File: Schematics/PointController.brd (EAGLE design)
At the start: 90 x 80 mm, 114 parts, among them IC1 MEGA48/88/168-AU

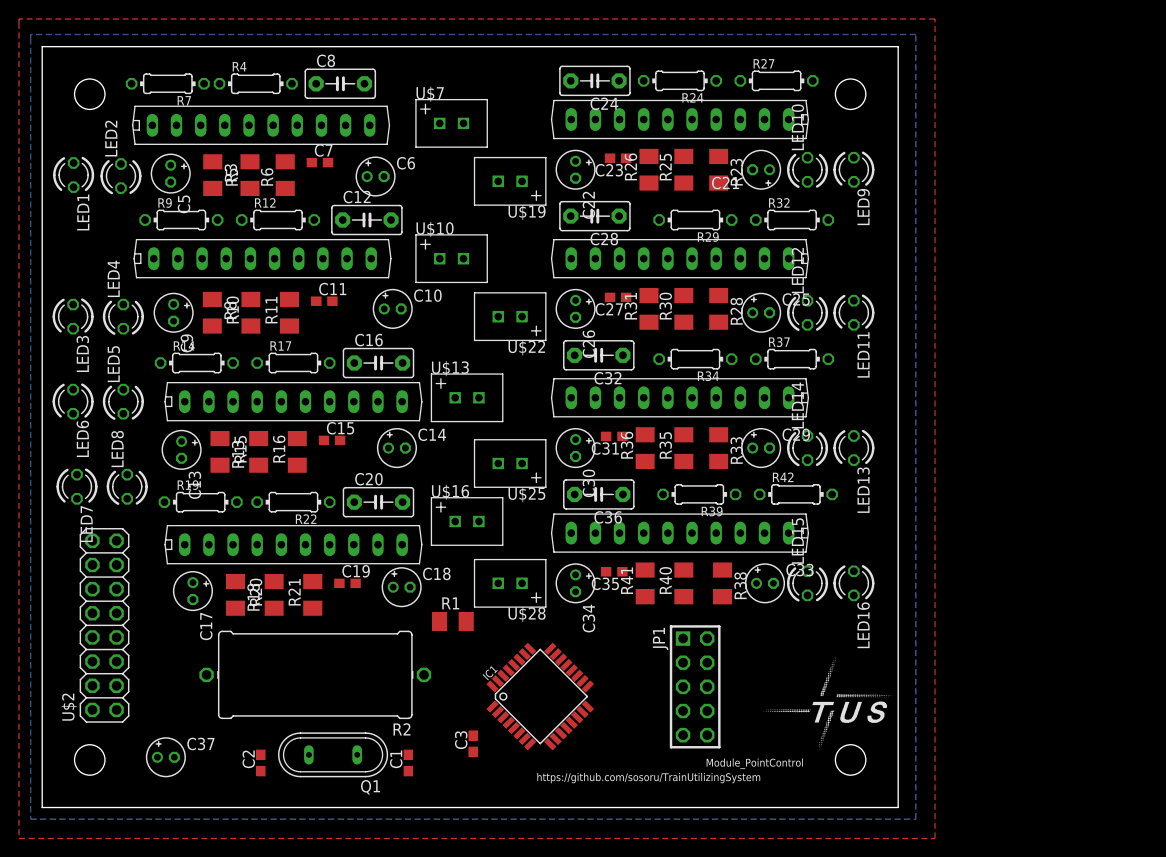
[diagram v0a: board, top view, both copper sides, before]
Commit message: create route test; board edit
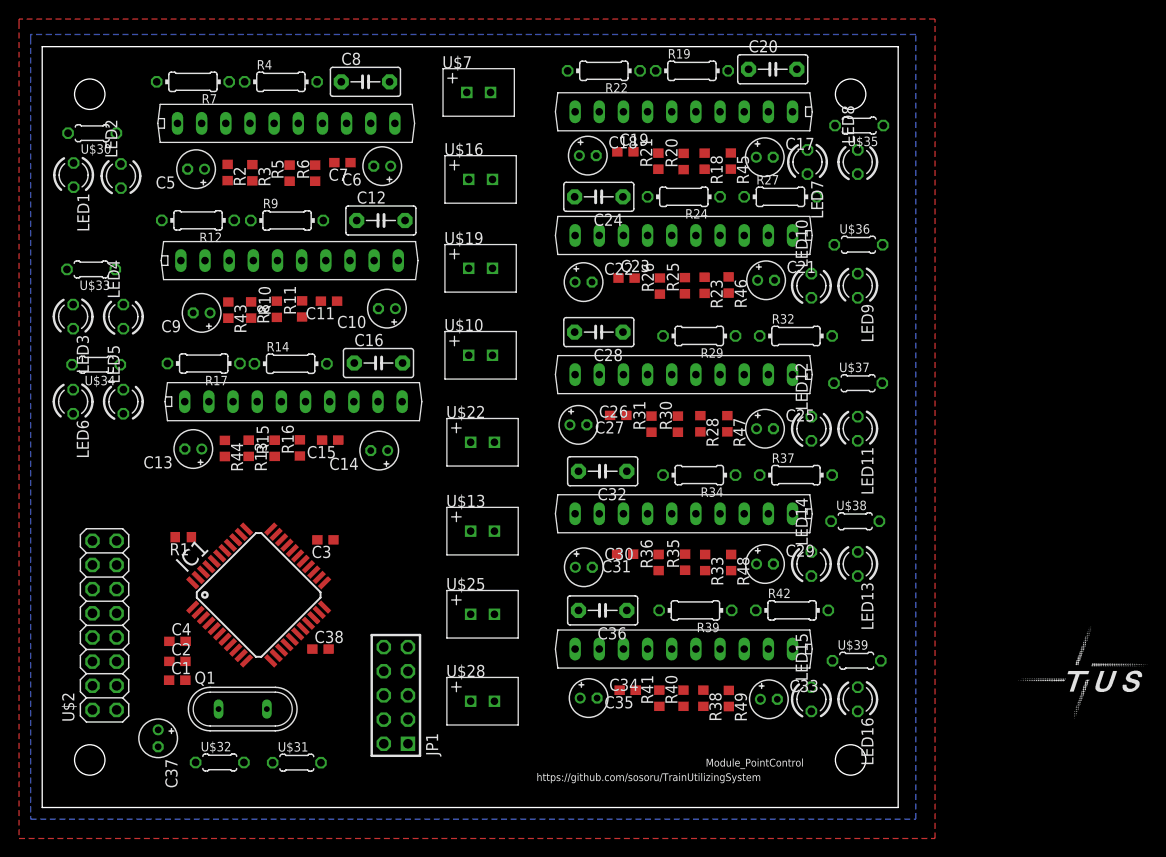
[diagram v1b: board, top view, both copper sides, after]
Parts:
- added C38, C4: (no value), rcl:C1608
- added R43, R44, R45, R46, R47, R48, R49: 100k, rcl:R0603
- added U$30, U$31, U$32, U$33, U$34, U$35, U$36, U$37, U$38, U$39: POLYSWITCH_20204/5, myparts:0204/5
- IC1: value MEGA48/88/168-AU -> MEGA164P/324P/644P-AU; device avr-7:TQFP32-08 -> avr-7:TQFP44
- JP1: value AVR-ISP-10 -> AVR-JTAG-10; device avr-7:AVR-ISP-10 -> avr-7:AVR-JTAG-10
- R1, R13, R18, R23, R28, R3, R33, R38, R8: device rcl:M3216 -> rcl:R0603
- R10, R11, R15, R16, R20, R21, R25, R26, R30, R31, R35, R36, R40, R41, R5, R6: value 10k -> 100k; device rcl:M3216 -> rcl:R0603
- R2: value (none) -> 100k; device rcl:0922/22 -> rcl:R0603
- moved LED7 84.1 mm to (80.5, 67.9)
- moved LED8 84.1 mm to (85.8, 67.9)
- moved C17 75.5 mm to (76.0, 68.4), turned to 0 degrees
- moved R19 68.7 mm to (68.3, 77.5)
- moved R18 67.2 mm to (69.6, 68.0)
- moved R20 62.7 mm to (67.4, 67.9)
- moved C20 61.6 mm to (76.8, 77.6)
- moved U$14 61.3 mm to (67.5, 73.2), turned to 180 degrees
- moved R21 58.3 mm to (64.8, 68.0)
- moved R22 55.9 mm to (59.1, 77.5)
- moved C19 54.0 mm to (61.3, 68.9)
- moved R2 53.6 mm to (19.5, 66.8), turned to 270 degrees
- moved C18 49.4 mm to (57.4, 68.5)
- moved U$16 36.0 mm to (47.3, 66.0)
- moved JP1 31.5 mm to (37.2, 11.8), turned to 90 degrees
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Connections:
- removed net PT_PWR: C10.+, C14.+, C18.+, C22.+, C26.+, C30.+, C34.+, C6.+, R13.2, R18.2, R2.1, R23.2, R28.2, R3.2, R33.2, R38.2, R8.2, U$1.8, U$11.8, U$14.8, U$17.8, U$20.8, U$23.8, U$26.8, U$8.8
- new net AREF: IC1.29
- new net N$43: U$2.1, U$2.2, U$2.4, U$31.1
- new net N$44: C37.+, U$2.6, U$32.1
- new net N$45: C6.+, R3.2, U$1.8, U$30.1
- new net N$46: C14.+, R13.2, U$11.8, U$34.1
- new net N$47: C22.+, R23.2, U$17.8, U$36.1
- new net N$48: C30.+, R33.2, U$23.8, U$38.1
- new net N$49: C34.+, R38.2, U$26.8, U$39.1
- new net N$50: C26.+, R28.2, U$20.8, U$37.1
- new net N$51: C18.+, R18.2, U$14.8, U$35.1
- new net N$52: C10.+, R8.2, U$33.1, U$8.8
- new net TCK: IC1.21, JP1.1
- new net TDI: IC1.24, JP1.9
- new net TDO: IC1.23, JP1.3
- new net TMS: IC1.22, JP1.5
- net !RESET: now also IC1.4, JP1.6; no longer IC1.29, JP1.5
- net !SS: now also IC1.44; no longer IC1.14
- net +12V: now also U$30.2, U$31.2, U$33.2, U$34.2, U$35.2, U$36.2, U$37.2, U$38.2, U$39.2; no longer R2.2, U$2.1, U$2.2, U$2.4
- net 5V: now also C38.1, C4.1, IC1.17, IC1.27, IC1.38, IC1.5, JP1.4, JP1.7, U$32.2; no longer C37.+, IC1.18, IC1.4, IC1.6, JP1.2, U$2.6
- net GND: now also C38.2, C4.2, IC1.18, IC1.28, IC1.39, IC1.6, JP1.2, R2.2, R43.2, R44.2, R45.2, R46.2, R47.2, R48.2, R49.2; no longer IC1.21, IC1.3, IC1.5, JP1.3, JP1.4, JP1.6, JP1.8
- net MISO: now also IC1.2; no longer IC1.16, JP1.9
- net MOSI: now also IC1.1; no longer IC1.15, JP1.1
- net N$13: now also R44.1
- net N$18: now also R45.1
- net N$2: now also R43.1
- net N$23: now also R46.1
- net N$28: now also R47.1
- net N$33: now also R48.1
- net N$38: now also R49.1
- net N$6: now also R2.1
- net OUT_A_0: now also IC1.37; no longer IC1.23
- net OUT_A_1: now also IC1.36; no longer IC1.24
- net OUT_B_0: now also IC1.35; no longer IC1.25
- net OUT_B_1: now also IC1.34; no longer IC1.26
- net OUT_C_0: now also IC1.33; no longer IC1.27
- net OUT_C_1: now also IC1.32; no longer IC1.28
- net OUT_D_0: now also IC1.31; no longer IC1.30
- net OUT_D_1: now also IC1.30; no longer IC1.31
- net OUT_E_0: now also IC1.9; no longer IC1.32
- net OUT_E_1: now also IC1.10; no longer IC1.1
- net OUT_F_0: now also IC1.11; no longer IC1.2
- net OUT_F_1: now also IC1.12; no longer IC1.9
- net OUT_G_0: now also IC1.13; no longer IC1.10
- net OUT_G_1: now also IC1.14; no longer IC1.11
- net OUT_H_0: now also IC1.15; no longer IC1.12
- net OUT_H_1: now also IC1.16; no longer IC1.13
- net SCK: now also IC1.3; no longer IC1.17, JP1.7

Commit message: restoring
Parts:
- removed C32, C36: (no value), capacitor-wima:C5B3
- removed C33: 10u, resistor:E1,8-4
- removed C34, C37: 47u, resistor:E1,8-4
- removed C35: 0.1u, rcl:C1608
- removed C38: (no value), rcl:C1608
- removed U$1, U$11, U$14, U$17, U$20, U$23, U$26, U$8: TA7291, TA7291P:HSIP10
- removed U$10, U$13, U$16, U$19, U$22, U$25, U$28, U$7: XH-2, myparts:XH-2
- removed U$2: TUS_MODULE_SUPPLY, myparts:2X08
- removed U$30, U$31, U$32, U$33, U$34, U$35, U$36, U$37, U$38, U$39: POLYSWITCH_20204/5, myparts:0204/5
- added A, B, C, D, E, F, G, H: XH-2, myparts:XH-2
- added C100, C101, C102, C103, C104, C105, C106, C107: 0.1u, rcl:C1608
- added CONN: TUS_MODULE_SUPPLY, myparts:2X08
- added F1, F2, F3, F4, F5, F6, F7, F8, F9: POLYSWITCH_20204/5, myparts:0204/5
- added IC2, IC3, IC4, IC5, IC7, IC8, IC9: TA7291, TA7291P:HSIP10
- added IC6: MEGA164P/324P/644P-AU, avr-7:TQFP44
- C1, C2: value (none) -> 47u; device rcl:C1608 -> capacitor-wima:C5B3
- C10, C14, C18, C30, C6: value 47u -> 0.1u; device resistor:E1,8-4 -> rcl:C1608
- C12, C28, C8: value (none) -> 47u
- C13, C29, C9: value 10u -> (none); device resistor:E1,8-4 -> rcl:E2,5-5
- C16, C24: device capacitor-wima:C5B3 -> rcl:E2,5-5
- C17, C25, C5: value 10u -> 0.1u; device resistor:E1,8-4 -> rcl:C1608
- C19, C7: value 0.1u -> 47u; device rcl:C1608 -> capacitor-wima:C5B3
- C20: value (none) -> 22p; device capacitor-wima:C5B3 -> rcl:C1608
- C21: value 10u -> 22p; device resistor:E1,8-4 -> rcl:C1608
- C22: device resistor:E1,8-4 -> rcl:E2,5-5
- C23: value 0.1u -> 47u; device rcl:C1608 -> rcl:E2,5-5
- C26: device resistor:E1,8-4 -> capacitor-wima:C5B3
- C27: value 0.1u -> (none); device rcl:C1608 -> rcl:E2,5-5
- C3, C4: device rcl:C1608 -> rcl:E2,5-5
- IC1: value MEGA164P/324P/644P-AU -> TA7291; device avr-7:TQFP44 -> TA7291P:HSIP10
- LED1, LED11, LED13, LED15, LED3, LED5, LED7, LED9: value (none) -> G
- LED10, LED12, LED14, LED16, LED2, LED4, LED6, LED8: value (none) -> O
- Q1: value (none) -> 20.000M
- R1: value (none) -> 10k; device rcl:R0603 -> resistor:0204/7
- R10, R21, R36, R46, R47: value 100k -> 1k; device rcl:R0603 -> resistor:R0603
- R12, R17, R24, R37, R42: value (none) -> 100k; device resistor:0204/7 -> rcl:R0603
- R13, R38: device rcl:R0603 -> resistor:0204/7
- R14, R32, R39: value (none) -> 10k
- R16, R31, R41, R43: value 100k -> 10k
- R18, R23, R28, R3, R33, R8: value 10k -> 100k
- R19, R27, R34, R4, R7: value (none) -> 10k; device resistor:0204/7 -> rcl:R0603
- R2, R25: value 100k -> 10k; device rcl:R0603 -> resistor:0204/7
- R22, R29, R9: value (none) -> 1k; device resistor:0204/7 -> resistor:R0603
- moved LED13 83.8 mm to (3.25, 11.2)
- moved C2 81.2 mm to (68.7, 75.6)
- moved LED1 78.2 mm to (81.5, 67.5)
- moved LED2 77.7 mm to (86.0, 67.5)
- moved C4 76.8 mm to (73.6, 66.2)
- moved LED14 74.2 mm to (8.13, 11.2)
- moved R45 73.5 mm to (25.4, 11.4), turned to 0 degrees
- moved C20 73.3 mm to (20.5, 30.7), turned to 180 degrees
- moved C17 67.7 mm to (17.7, 33.9)
- moved R47 66.2 mm to (13.0, 10.3), turned to 90 degrees
- moved C21 64.2 mm to (16.9, 30.6)
- moved C1 63.3 mm to (24.5, 75.8), turned to 180 degrees
- moved C27 58.5 mm to (6.10, 19.9), turned to 0 degrees
- moved C9 57.2 mm to (74.0, 52.0), turned to 0 degrees
- moved R18 53.7 mm to (18.2, 52.8), turned to 180 degrees
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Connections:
- removed net AREF: IC1.29
- removed net N$43: U$2.1, U$2.2, U$2.4, U$31.1
- net !RESET: now also CONN.15, IC6.4, R31.2; no longer IC1.4, R1.2, U$2.15
- net !SS: now also CONN.11, IC6.44; no longer IC1.44, U$2.11
- net +12V: now also C22.+, CONN.1, CONN.2, CONN.4, F1.2, F2.2, F3.2, F4.2, F5.2, F6.2, F8.2, F9.2; no longer U$30.2, U$31.2, U$33.2, U$34.2, U$35.2, U$36.2, U$37.2, U$38.2, U$39.2
- net 5V: now also C100.2, C101.2, C102.2, C103.2, C104.2, C105.2, C106.2, C107.2, C14.1, C17.1, C18.1, C23.+, F7.2, IC1.7, IC2.7, IC3.7, IC4.7, IC5.7, IC6.17, IC6.27, IC6.29, IC6.38, IC6.5, IC7.7, IC8.7, IC9.7, R31.1; no longer C11.2, C13.+, C15.2, C17.+, C19.2, C21.+, C23.2, C25.+, C27.2, C29.+, C3.1, C31.2, C33.+, C35.2, C38.1, C4.1, C5.+, C7.2, C9.+, IC1.17, IC1.27, IC1.38, IC1.5, R1.1, U$1.7, U$11.7, U$14.7, U$17.7, U$20.7, U$23.7, U$26.7, U$32.2, U$8.7
- net GND: now also C10.1, C100.1, C101.1, C102.1, C103.1, C104.1, C105.1, C106.1, C107.1, C14.2, C16.-, C17.2, C18.2, C20.1, C21.1, C23.-, C24.-, C25.1, C27.-, C3.-, C30.1, C4.-, C5.1, C6.1, CONN.12, CONN.3, CONN.5, CONN.7, CONN.8, CONN.9, IC1.1, IC2.1, IC3.1, IC4.1, IC5.1, IC6.18, IC6.28, IC6.39, IC6.6, IC7.1, IC8.1, IC9.1, R12.1, R15.2, R17.1, R18.2, R23.1, R24.1, R26.2, R28.1, R3.2, R33.2, R37.1, R40.2, R42.1, R45.1, R48.1, R49.1, R6.2, R8.1; no longer C1.1, C10.-, C14.-, C17.-, C18.-, C19.1, C2.1, C21.-, C23.1, C25.-, C26.-, C27.1, C3.2, C30.-, C33.-, C34.-, C35.1, C37.-, C38.2, C4.2, C5.-, C6.-, C7.1, IC1.18, IC1.28, IC1.39, IC1.6, R10.1, R15.1, R16.1, R2.2, R21.1, R25.1, R26.1, R31.1, R36.1, R40.1, R41.1, R43.2, R45.2, R46.2, R47.2, R48.2, R49.2, R6.1, U$1.1, U$11.1, U$14.1, U$17.1, U$2.12, U$2.3, U$2.5, U$2.7, U$2.8, U$2.9, U$20.1, U$23.1, U$26.1, U$8.1
- net MISO: now also CONN.14, IC6.2; no longer IC1.2, U$2.14
- net MOSI: now also CONN.16, IC6.1; no longer IC1.1, U$2.16
- net N$1: now also LED5.K, LED6.A, R22.2; no longer LED1.A, LED2.K, R7.2
- net N$10: now also B.P$1, IC1.10, R1.1, R10.1; no longer R12.1, R9.1, U$10.P$1, U$8.10
- net N$11: now also C1.1, R1.2; no longer C12.1, R9.2
- net N$12: now also LED3.K, LED4.A, R10.2; no longer LED3.A, LED4.K, R12.2
- net N$13: now also IC2.4, R3.1, R4.1; no longer R13.1, R44.1, U$11.4
- net N$14: now also C.P$2, C2.2, IC2.2, LED1.A, LED2.K; no longer C16.2, LED5.K, LED6.A, U$11.2, U$13.P$2
- net N$15: now also C.P$1, IC2.10, R2.1, R9.1; no longer R14.1, R17.1, U$11.10, U$13.P$1
- net N$16: now also C2.1, R2.2; no longer C16.1, R14.2
- net N$17: now also LED1.K, LED2.A, R9.2; no longer LED5.A, LED6.K, R17.2
- net N$18: now also IC3.4, R15.1, R16.1; no longer R18.1, R45.1, U$14.4
- net N$19: now also C8.2, D.P$2, IC3.2, LED7.A, LED8.K; no longer C20.2, LED7.K, LED8.A, U$14.2, U$16.P$2
- net N$2: now also IC1.4, R6.1, R7.1; no longer R43.1, R8.1, U$8.4
- net N$20: now also D.P$1, IC3.10, R14.1, R21.1; no longer R19.1, R22.1, U$14.10, U$16.P$1
- net N$21: now also C8.1, R14.2; no longer C20.1, R19.2
- net N$22: now also LED7.K, LED8.A, R21.2; no longer LED7.A, LED8.K, R22.2
- net N$23: now also IC9.4, R43.1, R44.1; no longer R23.1, R46.1, U$17.4
- net N$24: now also C26.2, E.P$2, IC9.2, LED13.A, LED14.K; no longer C24.2, LED10.A, LED9.K, U$17.2, U$19.P$2
- net N$25: now also E.P$1, IC9.10, R38.1, R47.1; no longer R24.1, R27.1, U$17.10, U$19.P$1
- net N$26: now also C26.1, R38.2; no longer C24.1, R24.2
- net N$27: now also LED13.K, LED14.A, R47.2; no longer LED10.K, LED9.A, R27.2
- net N$28: now also IC8.4, R40.1, R41.1; no longer R28.1, R47.1, U$20.4
- net N$29: now also F.P$2, IC8.2, LED15.A, LED16.K; no longer LED11.K, LED12.A, U$20.2, U$22.P$2
- net N$3: now also C20.2, IC6.8; no longer C1.2, IC1.8
- net N$30: now also F.P$1, IC8.10, R39.1, R46.1; no longer R29.1, R32.1, U$20.10, U$22.P$1
- net N$31: now also R39.2; no longer R29.2
- net N$32: now also LED15.K, LED16.A, R46.2; no longer LED11.A, LED12.K, R32.2
- net N$33: now also IC7.4, R34.1; no longer R48.1, U$23.4
- net N$34: now also C19.2, G.P$2, IC7.2, LED11.A, LED12.K; no longer C32.2, LED13.K, LED14.A, U$23.2, U$25.P$2
- net N$35: now also G.P$1, IC7.10, R32.1, R36.1; no longer R34.1, R37.1, U$23.10, U$25.P$1
- net N$36: now also C19.1, R32.2; no longer C32.1, R34.2
- net N$37: now also LED11.K, LED12.A, R36.2; no longer LED13.A, LED14.K, R37.2
- net N$38: now also IC5.4, R26.1, R27.1; no longer R38.1, R49.1, U$26.4
- net N$39: now also C12.2, H.P$2, IC5.2, LED10.K, LED9.A; no longer C36.2, LED15.K, LED16.A, U$26.2, U$28.P$2
- net N$4: now also C21.2, IC6.7; no longer C2.2, IC1.7
- net N$40: now also H.P$1, IC5.10, R25.1, R29.1; no longer R39.1, R42.1, U$26.10, U$28.P$1
- net N$41: now also C12.1, R25.2; no longer C36.1, R39.2
- net N$42: now also LED10.A, LED9.K, R29.2; no longer LED15.A, LED16.K, R42.2
- net N$44: now also CONN.6, F7.1; no longer C37.+, U$2.6, U$32.1
- net N$45: now also C11.2, C13.+, F3.1, IC4.8, R19.2; no longer C6.+, R3.2, U$1.8, U$30.1
- net N$46: now also C4.+, C5.2, F2.1, IC2.8, R4.2; no longer C14.+, R13.2, U$11.8, U$34.1
- net N$47: now also C27.+, C31.2, F8.1, IC9.8, R43.2; no longer C22.+, R23.2, U$17.8, U$36.1
- net N$48: now also C24.+, C25.2, F6.1, IC7.8, R34.2; no longer C30.+, R33.2, U$23.8, U$38.1
- net N$49: now also C15.2, C16.+, F5.1, IC5.8, R27.2; no longer C34.+, R38.2, U$26.8, U$39.1
- net N$5: now also B.P$2, C1.2, IC1.2, LED3.A, LED4.K; no longer C12.2, LED3.K, LED4.A, U$10.P$2, U$8.2
- net N$50: now also C29.+, C30.2, F9.1, IC8.8, R41.2; no longer C26.+, R28.2, U$20.8, U$37.1
- net N$51: now also C10.2, C9.+, F4.1, IC3.8, R16.2; no longer C18.+, R18.2, U$14.8, U$35.1
- net N$52: now also C3.+, C6.2, F1.1, IC1.8, R7.2; no longer C10.+, R8.2, U$33.1, U$8.8
- net N$6: now also IC4.4, R18.1, R19.1; no longer R2.1, R3.1, U$1.4
- net N$7: now also A.P$2, C7.2, IC4.2, LED5.A, LED6.K; no longer C8.2, LED1.K, LED2.A, U$1.2, U$7.P$2
- net N$8: now also A.P$1, IC4.10, R13.1, R22.1; no longer R4.1, R7.1, U$1.10, U$7.P$1
- net N$9: now also C7.1, R13.2; no longer C8.1, R4.2
- net OUT_A_0: now also IC4.5, IC6.37, R20.2; no longer IC1.37, R5.2, U$1.5
- net OUT_A_1: now also IC4.6, IC6.36, R24.2; no longer IC1.36, R6.2, U$1.6
- net OUT_B_0: now also IC1.5, IC6.35, R12.2; no longer IC1.35, R10.2, U$8.5
- net OUT_B_1: now also IC1.6, IC6.34, R8.2; no longer IC1.34, R11.2, U$8.6
- net OUT_C_0: now also IC2.5, IC6.33, R5.2; no longer IC1.33, R15.2, U$11.5
- net OUT_C_1: now also IC2.6, IC6.32, R11.2; no longer IC1.32, R16.2, U$11.6
- net OUT_D_0: now also IC3.5, IC6.31, R17.2; no longer IC1.31, R20.2, U$14.5
- net OUT_D_1: now also IC3.6, IC6.30, R23.2; no longer IC1.30, R21.2, U$14.6
- net OUT_E_0: now also IC6.9, IC9.5, R45.2; no longer IC1.9, R25.2, U$17.5
- net OUT_E_1: now also IC6.10, IC9.6, R49.2; no longer IC1.10, R26.2, U$17.6
- net OUT_F_0: now also IC6.11, IC8.5, R48.2; no longer IC1.11, R30.2, U$20.5
- net OUT_F_1: now also IC6.12, IC8.6, R42.2; no longer IC1.12, R31.2, U$20.6
- net OUT_G_0: now also IC6.13, IC7.5, R37.2; no longer IC1.13, R35.2, U$23.5
- net OUT_G_1: now also IC6.14, IC7.6, R35.2; no longer IC1.14, R36.2, U$23.6
- net OUT_H_0: now also IC5.5, IC6.15, R30.2; no longer IC1.15, R40.2, U$26.5
- net OUT_H_1: now also IC5.6, IC6.16, R28.2; no longer IC1.16, R41.2, U$26.6
- net SCK: now also CONN.13, IC6.3; no longer IC1.3, U$2.13
- net TCK: now also IC6.21; no longer IC1.21
- net TDI: now also IC6.24; no longer IC1.24
- net TDO: now also IC6.23; no longer IC1.23
- net TMS: now also IC6.22; no longer IC1.22
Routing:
- net 5V: track 0.00 -> 316.1 mm, vias 0 -> 1
- net +12V: track 0.00 -> 277.8 mm
- net GND: track 0.00 -> 187.5 mm, vias 0 -> 37
- net OUT_E_1: track 0.00 -> 74.3 mm, vias 0 -> 1
- net OUT_F_0: track 0.00 -> 71.3 mm, vias 0 -> 1
- net OUT_F_1: track 0.00 -> 64.3 mm
- net OUT_E_0: track 0.00 -> 62.4 mm
- net OUT_B_0: track 0.00 -> 62.2 mm
- net N$7: track 0.00 -> 59.7 mm, vias 0 -> 2
- net OUT_C_1: track 0.00 -> 58.8 mm
- net OUT_B_1: track 0.00 -> 58.3 mm
- net OUT_G_0: track 0.00 -> 57.4 mm, vias 0 -> 1
- net OUT_C_0: track 0.00 -> 55.6 mm
- net N$5: track 0.00 -> 55.0 mm
- net OUT_G_1: track 0.00 -> 51.5 mm
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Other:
- board text added: "A"
- board text added: "B"
- board text added: "C"
- board text added: "D"
- board text added: "D48245"
- board text added: "E"
- board text added: "F"
- board text added: "G"
- board text added: "H"
- board text added: "module_PointControl"
- board text removed: "Module_PointControl"
